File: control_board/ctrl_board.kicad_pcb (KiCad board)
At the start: 2 copper layers, 130 x 130 mm, 34 parts, among them J1 CONN_01X04, J2 CONN_01X02, J3 CONN_01X04, J4 CONN_01X04, J5 CONN_01X04, J6 CONN_01X04, J7 CONN_01X04, J8 CONN_01X04, U1 PCA9685PW, U2 MBI1801, U3 MBI1801, U4 MBI1801, U5 MBI1801, U6 MBI1801, U7 MBI1801

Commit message: ctrl_board: [wip] place and route
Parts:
- J3, J4, J5, J6, J7, J8: footprint generated:MicroMatch_4p -> generated:THT_MicroMatch_4p; moved to B.Cu
- moved R2 21.4 mm to (57.5, -11.7), turned to 0 degrees
- moved C4 18.8 mm to (57.5, -9.14), turned to 180 degrees
- moved C5 1.00 mm to (47.0, 9.58)
- turned J3 to 210 degrees
- turned J4 to 270 degrees
- turned J5 to 330 degrees
- turned J6 to 30 degrees
- turned J7 to 90 degrees
- turned J8 to 150 degrees
- turned U2 to 210 degrees
- turned U3 to 270 degrees
- turned U4 to 330 degrees
- turned U5 to 30 degrees
- turned U6 to 90 degrees
- turned U7 to 150 degrees
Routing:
- net VLED: track 0.00 -> 414.4 mm
- net N$9: track 0.00 -> 15.8 mm
- net N$3: track 0.50 -> 15.1 mm
- net N$7: track 0.00 -> 14.4 mm
- net N$1: track 0.00 -> 14.3 mm
- net N$5: track 0.00 -> 14.2 mm
- net N$11: track 0.00 -> 14.2 mm
- net N$2: track 5.70 -> 0.30 mm
- net GND: track 1.98 -> 6.39 mm
- net +5V: track 3.59 -> 5.53 mm
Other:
- net class Default: clearance 0.3048 -> 0.4064; trace_width 0.25 -> 0.4064
- net class vled added: clearance 0.508, trace_width 0.508, via_dia 0.6, via_drill 0.4
- rule trace_clearance: 0.3048 -> 0.4064

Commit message: ctrl_board: [wip] place and route
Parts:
- moved J1 22.9 mm to (11.7, 57.7), turned to 0 degrees
- moved C1 21.6 mm to (8.60, 50.3)
- moved R5 21.4 mm to (-57.5, 11.7), turned to 180 degrees
- moved R3 21.4 mm to (18.6, -55.6), turned to 60 degrees
- moved R6 21.4 mm to (-18.6, 55.6), turned to 240 degrees
- moved R1 21.4 mm to (38.9, 44.0), turned to 300 degrees
- moved R4 21.4 mm to (-38.9, -44.0), turned to 120 degrees
- moved C10 18.8 mm to (-57.5, 9.14), turned to 0 degrees
- moved C12 18.8 mm to (-20.8, 54.4), turned to 60 degrees
- moved C6 18.8 mm to (20.8, -54.4), turned to 240 degrees
- moved C2 18.8 mm to (36.7, 45.2), turned to 120 degrees
- moved C8 18.8 mm to (-36.7, -45.2), turned to 300 degrees
- moved C13 1.00 mm to (-31.8, 35.9)
- moved C7 1.00 mm to (31.8, -35.9)
- moved C3 1.00 mm to (15.2, 45.5)
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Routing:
- net +5V: track 5.53 -> 457.3 mm, vias 0 -> 7
- net CTRL3: track 0.00 -> 191.0 mm, vias 0 -> 2
- net CTRL4: track 0.00 -> 154.5 mm, vias 0 -> 2
- net CTRL2: track 0.00 -> 128.2 mm, vias 0 -> 2
- net CTRL5: track 0.00 -> 95.5 mm, vias 0 -> 2
- net GND: track 6.39 -> 62.2 mm
- net CTRL1: track 0.00 -> 46.4 mm, vias 0 -> 2
- net CTRL6: track 0.00 -> 32.5 mm, vias 0 -> 2
- net SDA: track 0.00 -> 14.9 mm
- net SCL: track 0.00 -> 14.1 mm
- net VLED: track 414.4 -> 425.2 mm
- net N$4: track 0.00 -> 8.06 mm
- net N$10: track 0.00 -> 7.61 mm
- net N$12: track 0.00 -> 5.84 mm
- net N$2: track 0.30 -> 5.46 mm
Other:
- net class Default: clearance 0.4064 -> 0.3047; trace_width 0.4064 -> 0.3047
- rule trace_clearance: 0.4064 -> 0.3047

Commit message: ctrl_board: [wip] place and route
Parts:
- moved C13 19.8 mm to (-16.0, 47.9), turned to 60 degrees
- moved C7 19.8 mm to (16.0, -47.9), turned to 240 degrees
- moved C3 19.8 mm to (33.5, 37.8), turned to 120 degrees
- moved C9 19.8 mm to (-33.5, -37.8), turned to 300 degrees
- moved C11 19.8 mm to (-49.5, 10.1), turned to 0 degrees
- moved C5 19.8 mm to (49.5, -10.1), turned to 180 degrees
- moved J2 0.06 mm to (2.54, 60.0)
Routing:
- net VLED: track 425.2 -> 423.3 mm
- added copper zone on B.Cu, net GND
- added copper zone on F.Cu, net GND
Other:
- outline, holes or cut-outs redrawn

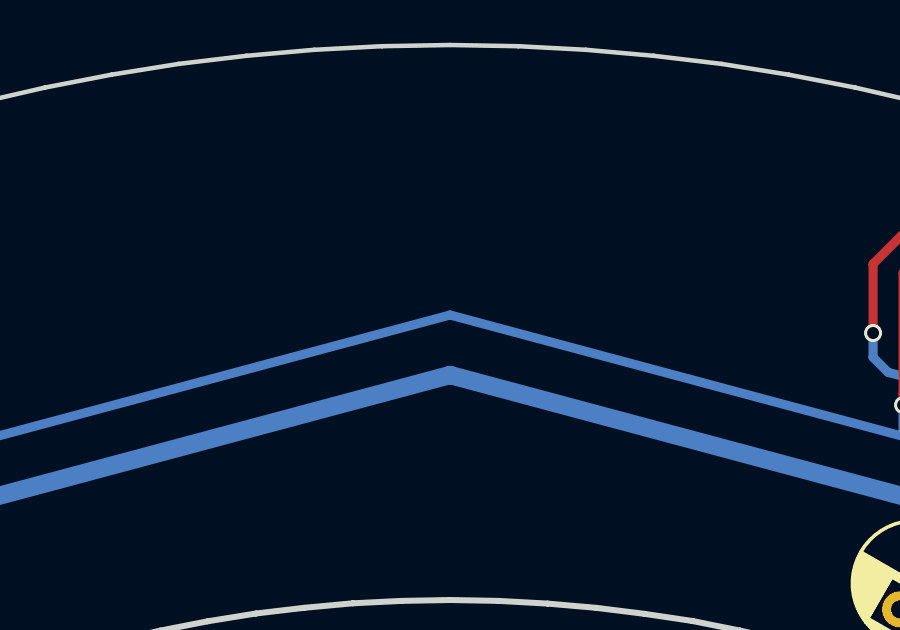
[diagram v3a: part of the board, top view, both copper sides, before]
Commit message: ctrl_board: Open Hardware logo
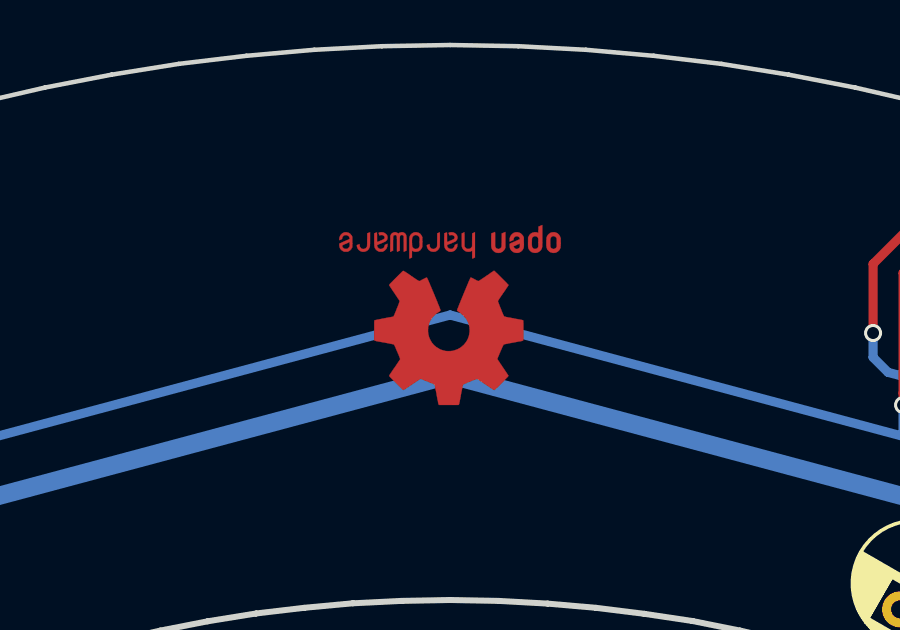
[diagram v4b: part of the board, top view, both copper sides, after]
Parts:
- added G2: LOGO, UGL:OSHW_Logo_6mm_height_BCu, F.Cu at (0.00, -56.0)

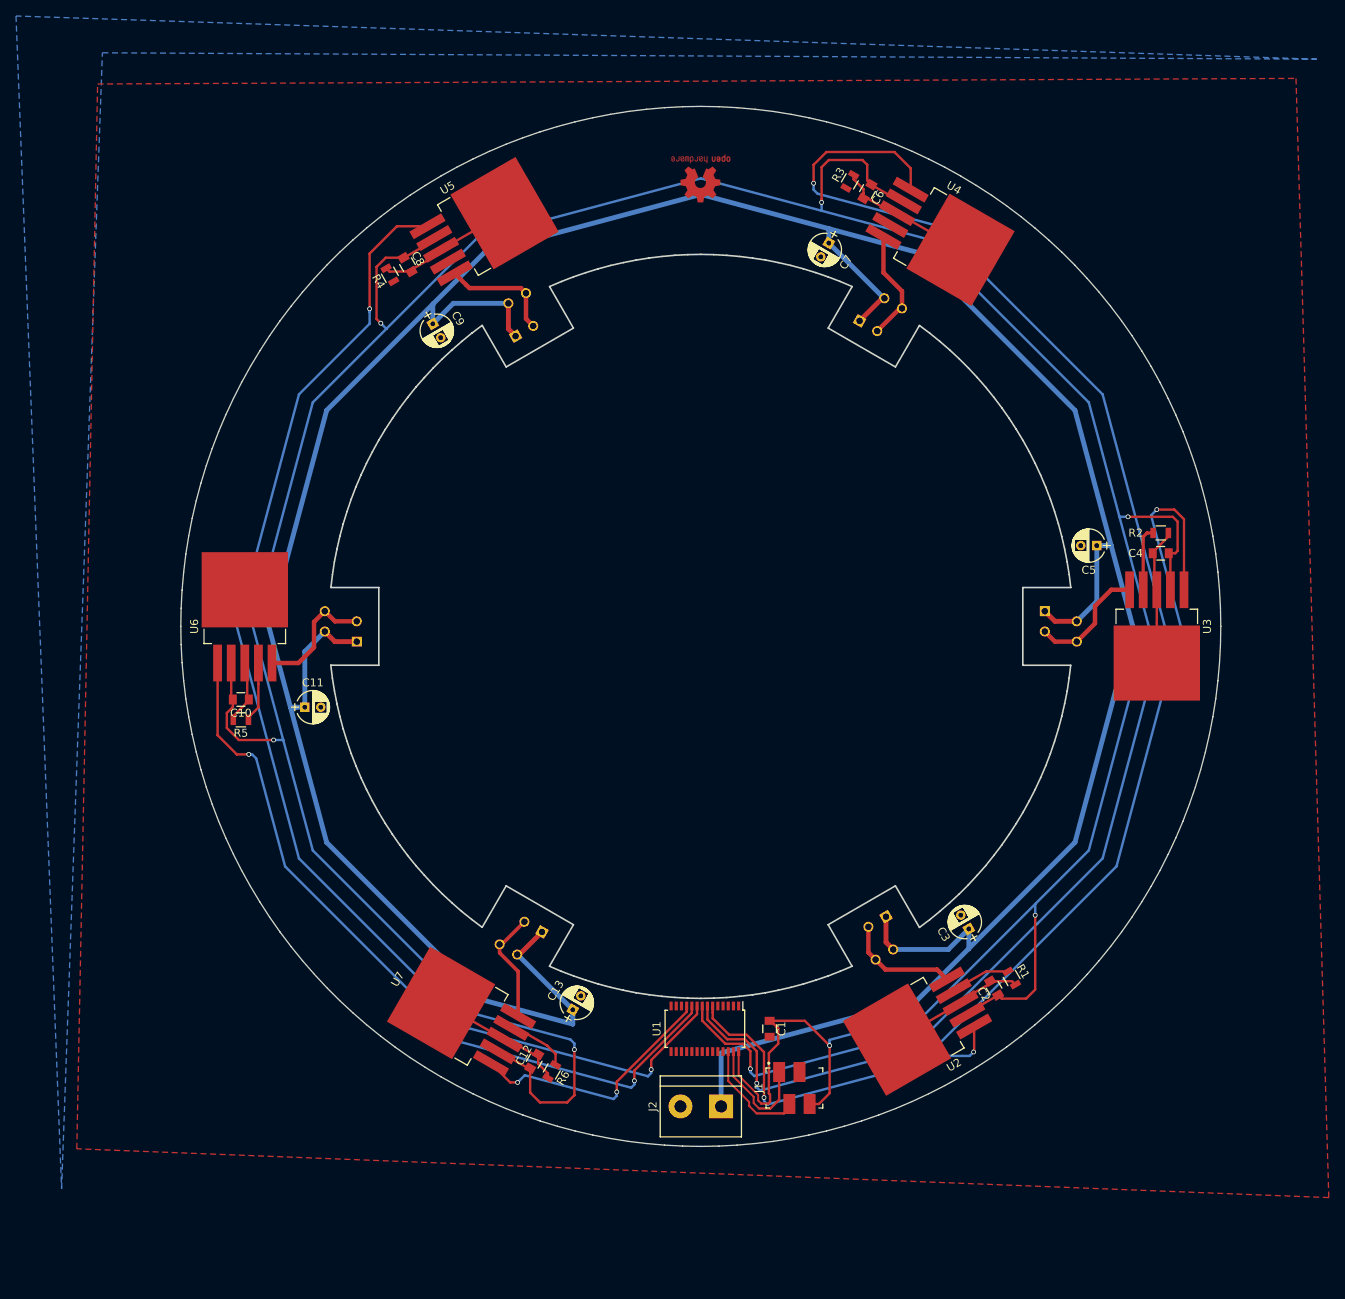
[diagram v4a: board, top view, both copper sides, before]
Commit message: ki_scripts: simple circle pattern
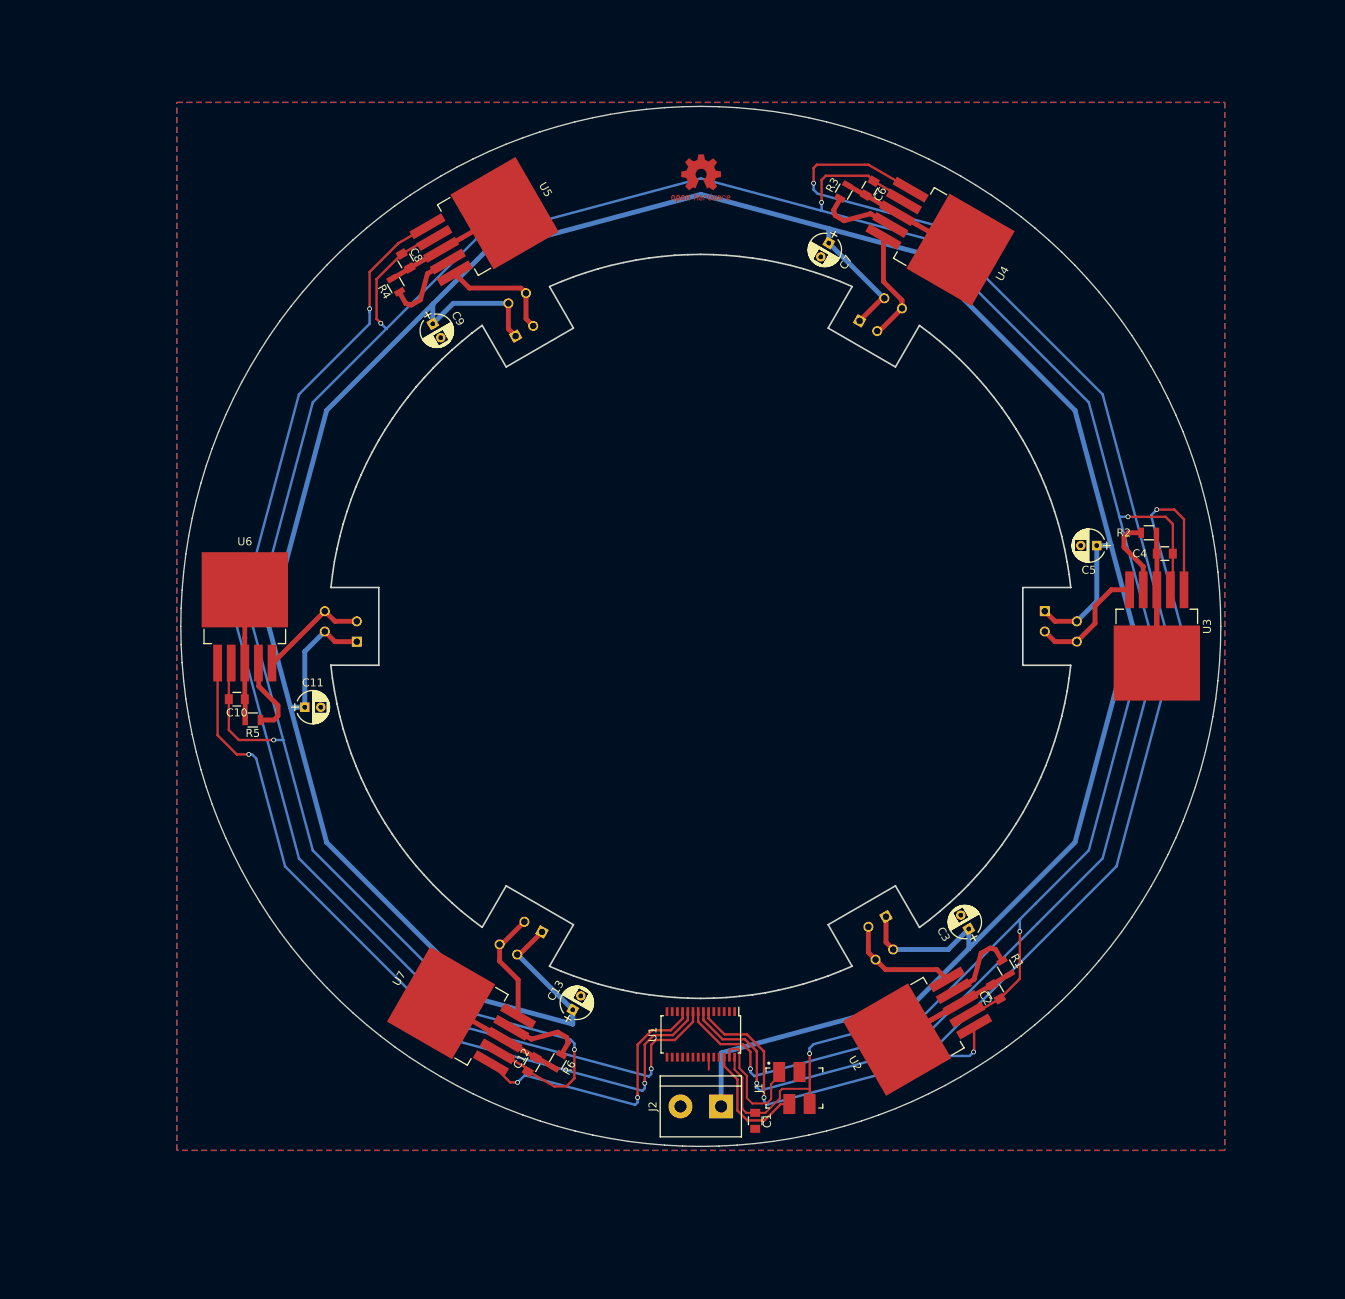
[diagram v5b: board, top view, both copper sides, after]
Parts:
- moved C1 11.6 mm to (6.80, 61.8)
- moved R2 1.49 mm to (56.0, -11.7)
- moved R1 1.49 mm to (38.1, 42.6)
- moved R4 1.49 mm to (-38.1, -42.6)
- moved R5 1.49 mm to (-56.0, 11.7)
- moved R3 1.49 mm to (17.9, -54.4)
- moved R6 1.49 mm to (-17.9, 54.4)
- moved U1 0.86 mm to (0.00, 51.0)
- moved C10 0.51 mm to (-58.0, 9.10)
- moved C4 0.51 mm to (58.0, -9.10)
- moved C12 0.51 mm to (-21.1, 54.8)
- moved C6 0.51 mm to (21.1, -54.8)
- moved C2 0.51 mm to (36.9, 45.7)
- moved C8 0.51 mm to (-36.9, -45.7)
- turned G2 to 0 degrees
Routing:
- net GND: track 62.2 -> 114.4 mm
- net +5V: track 457.3 -> 433.7 mm
- net N$6: track 0.00 -> 9.97 mm
- net N$8: track 0.00 -> 9.97 mm
- net CTRL3: track 191.0 -> 185.4 mm
- net N$2: track 5.46 -> 9.97 mm
- net N$12: track 5.84 -> 9.97 mm
- net CTRL6: track 32.5 -> 35.4 mm
- net N$10: track 7.61 -> 9.97 mm
- net N$9: track 15.8 -> 13.8 mm
- net N$4: track 8.06 -> 9.97 mm
- net CTRL5: track 95.5 -> 97.2 mm
- net SCL: track 14.1 -> 15.2 mm
- net CTRL4: track 154.5 -> 153.4 mm
- net SDA: track 14.9 -> 16.0 mm
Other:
- net class vled: clearance 0.508 -> 0.381; trace_width 0.508 -> 0.6095

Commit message: control_board: pca9685: fix i2c addr
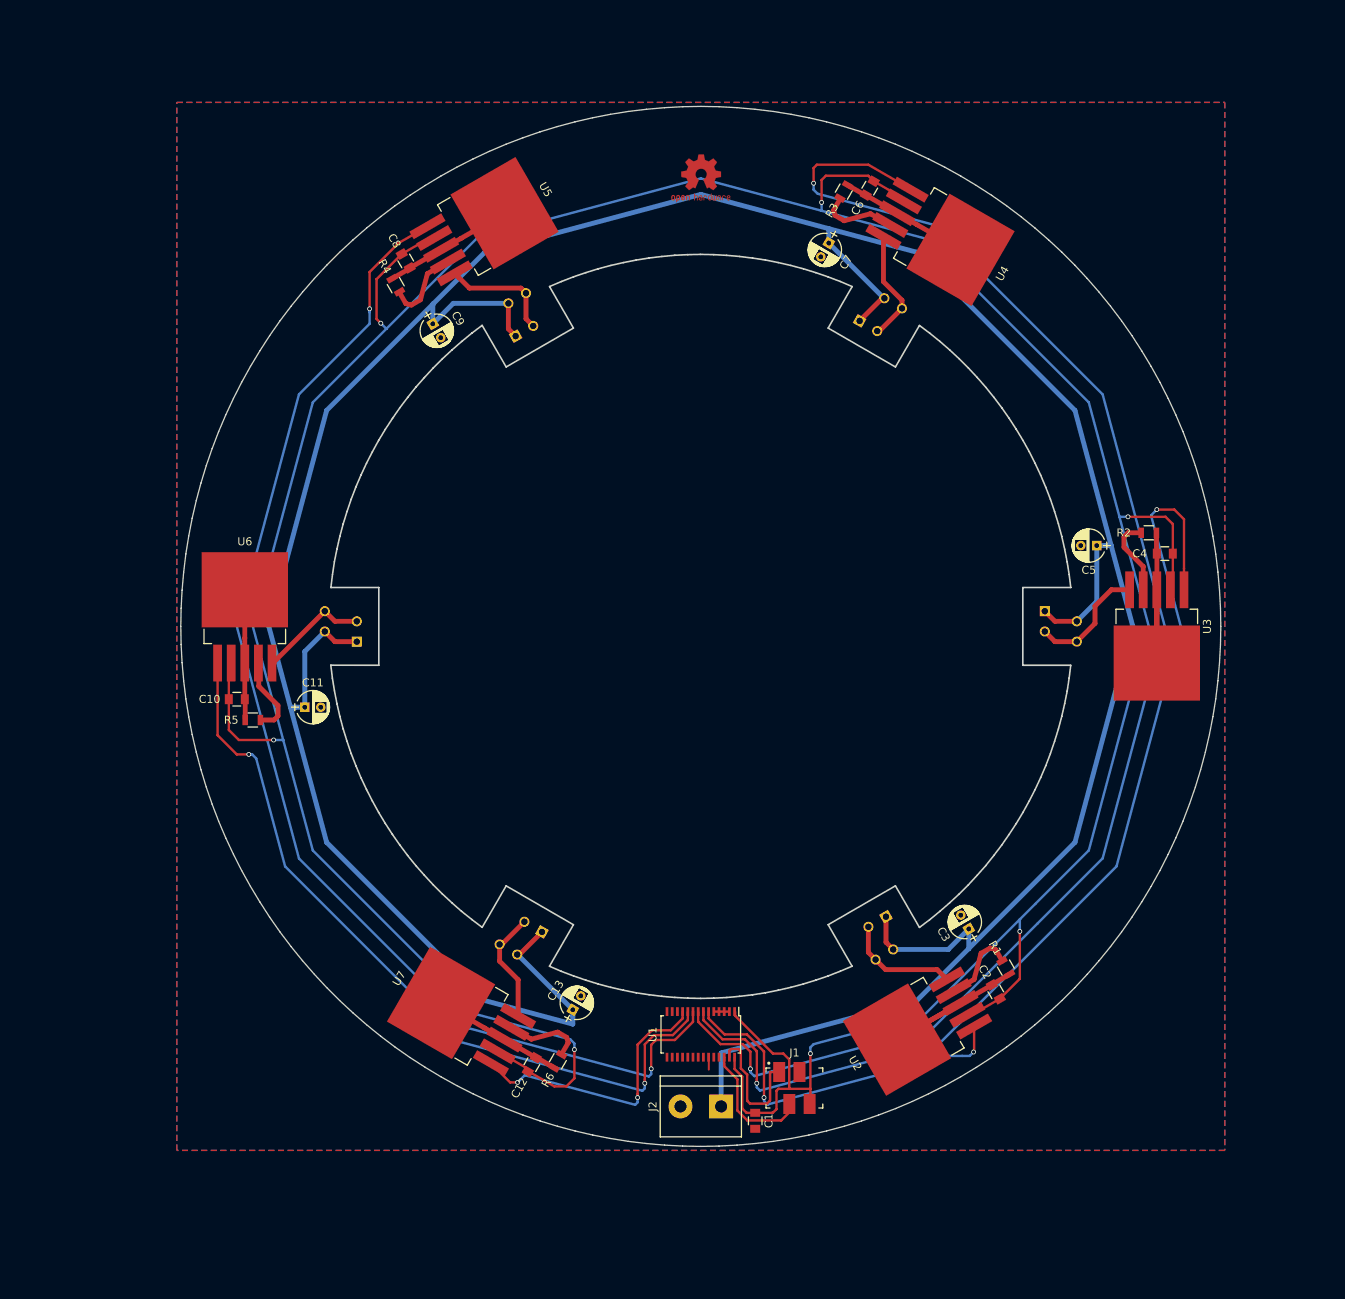
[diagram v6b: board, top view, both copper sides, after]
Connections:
- U1 pad 1: (no net) -> +5V
- U1 pad 2: (no net) -> GND
- U1 pad 3: (no net) -> GND
- U1 pad 4: (no net) -> GND
- U1 pad 5: (no net) -> GND
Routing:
- net +5V: track 433.7 -> 448.3 mm
- net GND: track 114.4 -> 116.2 mm
- net SDA: track 16.0 -> 16.8 mm
- net SCL: track 15.2 -> 15.8 mm

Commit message: ctrl_board: [wip] place and route
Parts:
- added REF**: , generated:Mounting_holes, F.Cu at (-48.4, 27.9)
- added REF**: , generated:Mounting_holes, F.Cu at (48.4, 27.9)
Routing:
- net GND: track 116.2 -> 131.8 mm
- net VLED: track 423.3 -> 416.5 mm
- net N$3: track 15.1 -> 13.1 mm
- net N$7: track 14.4 -> 13.5 mm
- net N$1: track 14.4 -> 13.5 mm
- net N$5: track 14.2 -> 13.4 mm
- net N$11: track 14.2 -> 13.4 mm
- net N$9: track 13.8 -> 13.2 mm
- net SDA: track 16.8 -> 16.2 mm
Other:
- outline, holes or cut-outs redrawn
- rule trace_min: 0.254 -> 0.3047
